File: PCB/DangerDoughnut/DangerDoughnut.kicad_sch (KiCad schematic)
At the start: 93 parts, among them J1 Conn_01x02_Pin, J2 Conn_01x02_Pin, J3 Conn_01x02_Pin, J4 Conn_01x04_Pin, J6 USB_C_Receptacle_USB2.0_16P, SW1 SW_Push, SW2 SW_Push, U1 MMC5983MA, U10 ESP32-S3, U2 H3LIS331DLTR, U3 H3LIS331DLTR, U4 W25X20CLZP, U6 L5973D, U7 MIC5219-3.3YM5, U8 ESP8285H16, U9 SX1280IMLTRT, Y1 40MHz, Y2 52MHz, Y3 26MHz

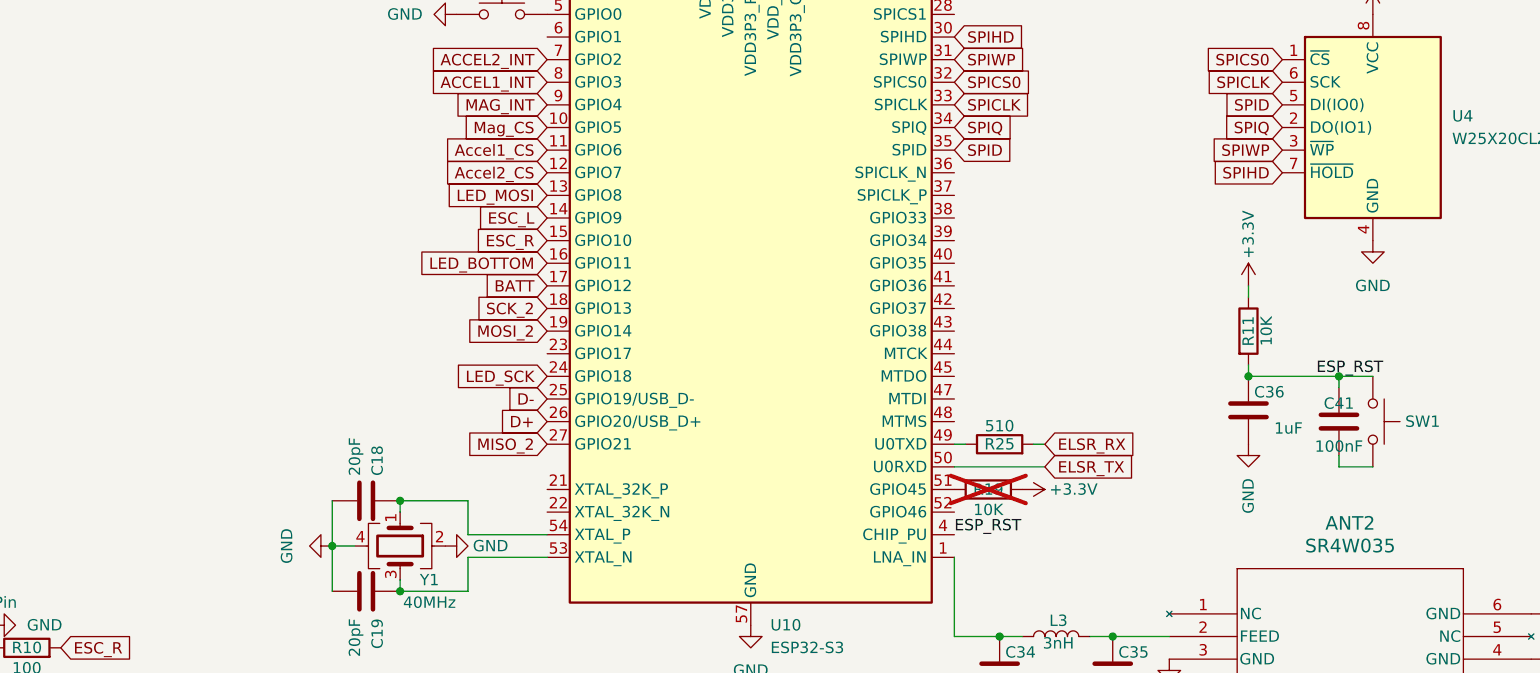
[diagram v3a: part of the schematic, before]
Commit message: updated layout
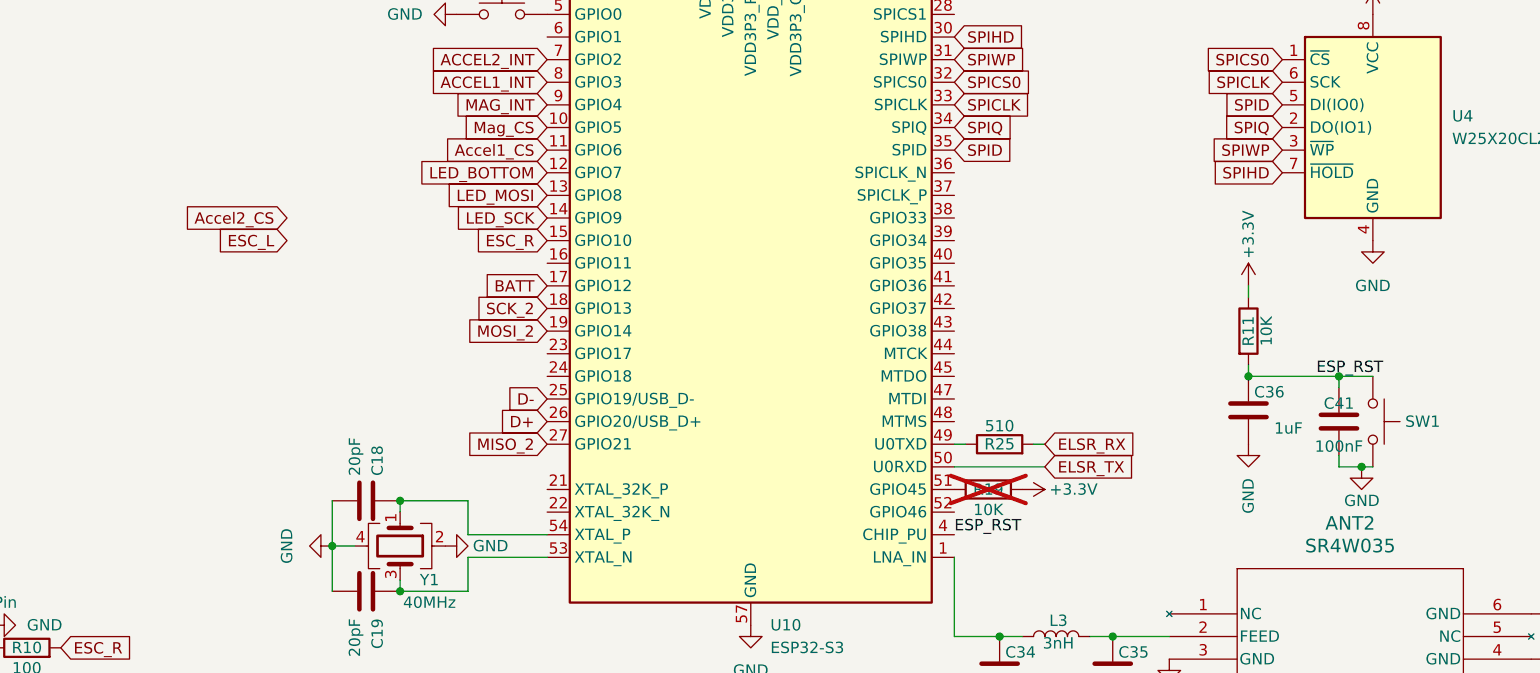
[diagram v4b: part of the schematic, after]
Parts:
- C29: footprint Capacitor_THT:CP_Radial_D6.3mm_P2.50mm -> Danger_Doughnut_Lib:CP_Right_Angle_D6.3_P2.50_H16.5
- SW1, SW2: footprint Button_Switch_SMD:SW_Push_1P1T_XKB_TS-1187A -> Danger_Doughnut_Lib:Pad_Button
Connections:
- net Accel2_CS: no longer U10.12 (GPIO7)
- net ESC_L: no longer U10.14 (GPIO9)
- net GND: now also C41.2, SW1.2
- net LED_BOTTOM: now also U10.12 (GPIO7); no longer U10.16 (GPIO11)
- net LED_SCK: now also U10.14 (GPIO9); no longer U10.24 (GPIO18)
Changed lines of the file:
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@@
 	)
 	(junction
+		(at 383.54 87.63)
+		(diameter 0)
+		(color 0 0 0 0)
+	)
+	(junction
 		(at 121.92 110.49)
 		(diameter 0)
@@
 	(wire
 		(pts
-			(xy 381 87.63) (xy 384.81 87.63)
+			(xy 381 87.63) (xy 383.54 87.63)
 		)
 		(stroke
@@
 	(wire
 		(pts
+			(xy 383.54 87.63) (xy 384.81 87.63)
+		)
+		(stroke
+			(width 0)
+			(type default)
+		)
+	)
+	(wire
+		(pts
 			(xy 318.77 222.25) (xy 317.5 222.25)
 		)
@@
 	(global_label "LED_BOTTOM"
 		(shape input)
-		(at 292.1 64.77 180)
+		(at 292.1 54.61 180)
 		(fields_autoplaced yes)
 		(effects
@@
 		)
 		(property "Intersheetrefs" "${INTERSHEET_REFS}"
-			(at 277.3825 64.77 0)
+			(at 277.3825 54.61 0)
 			(effects
 				(font
@@
 	(global_label "ESC_L"
 		(shape input)
-		(at 292.1 59.69 180)
+		(at 262.89 62.23 180)
 		(fields_autoplaced yes)
 		(effects
@@
 		)
 		(property "Intersheetrefs" "${INTERSHEET_REFS}"
-			(at 283.4906 59.69 0)
+			(at 254.2806 62.23 0)
 			(effects
 				(font
@@
 	(global_label "Accel2_CS"
 		(shape input)
-		(at 292.1 54.61 180)
+		(at 262.89 59.69 180)
 		(fields_autoplaced yes)
 		(effects
@@
 		)
 		(property "Intersheetrefs" "${INTERSHEET_REFS}"
-			(at 279.4386 54.61 0)
+			(at 250.2286 59.69 0)
 			(effects
 				(font
@@
 	(global_label "LED_SCK"
 		(shape input)
-		(at 292.1 77.47 180)
+		(at 292.1 59.69 180)
 		(fields_autoplaced yes)
 		(effects
@@
 		)
 		(property "Intersheetrefs" "${INTERSHEET_REFS}"
-			(at 280.9506 77.47 0)
+			(at 280.9506 59.69 0)
 			(effects
 				(font
@@
 			)
 		)
-		(property "Footprint" "Capacitor_THT:CP_Radial_D6.3mm_P2.50mm"
+		(property "Footprint" "Danger_Doughnut_Lib:CP_Right_Angle_D6.3_P2.50_H16.5"
 			(at 58.1152 224.79 0)
 			(effects
@@
 	)
 	(symbol
+		(lib_id "power:GND")
+		(at 383.54 87.63 0)
+		(unit 1)
+		(exclude_from_sim no)
+		(in_bom yes)
+		(on_board yes)
+		(dnp no)
+		(property "Reference" "#PWR0105"
+			(at 383.54 93.98 0)
+			(effects
+				(font
+					(size 1.27 1.27)
+				)
+				(hide yes)
+			)
+		)
+		(property "Value" "GND"
+			(at 385.572 91.44 0)
+			(effects
+				(font
+					(size 1.27 1.27)
+				)
+				(justify right)
+			)
+		)
+		(property "Footprint" ""
+			(at 383.54 87.63 0)
+			(effects
+				(font
+					(size 1.27 1.27)
+				)
+				(hide yes)
+			)
+		)
+		(property "Datasheet" ""
+			(at 383.54 87.63 0)
+			(effects
+				(font
+					(size 1.27 1.27)
+				)
+				(hide yes)
+			)
+		)
+		(property "Description" "Power symbol creates a global label with name \"GND\" , ground"
+			(at 383.54 87.63 0)
+			(effects
+				(font
+					(size 1.27 1.27)
+				)
+				(hide yes)
+			)
+		)
+		(pin "1"
+		)
+		(instances
+			(project "DangerDoughnut"
+				(path "/4036fe7f-48e1-40e6-b3b7-d8935a605c7b"
+					(reference "#PWR0105")
+					(unit 1)
+				)
+			)
+		)
+	)
+	(symbol
 		(lib_id "Device:C")
 		(at 353.06 22.86 0)
@@
 			)
 		)
-		(property "Footprint" "Button_Switch_SMD:SW_Push_1P1T_XKB_TS-1187A"
+		(property "Footprint" "Danger_Doughnut_Lib:Pad_Button"
 			(at 287.02 31.75 0)
 			(effects
@@
 			)
 		)
-		(property "Footprint" "Button_Switch_SMD:SW_Push_1P1T_XKB_TS-1187A"
+		(property "Footprint" "Danger_Doughnut_Lib:Pad_Button"
 			(at 389.89 82.55 0)
 			(effects

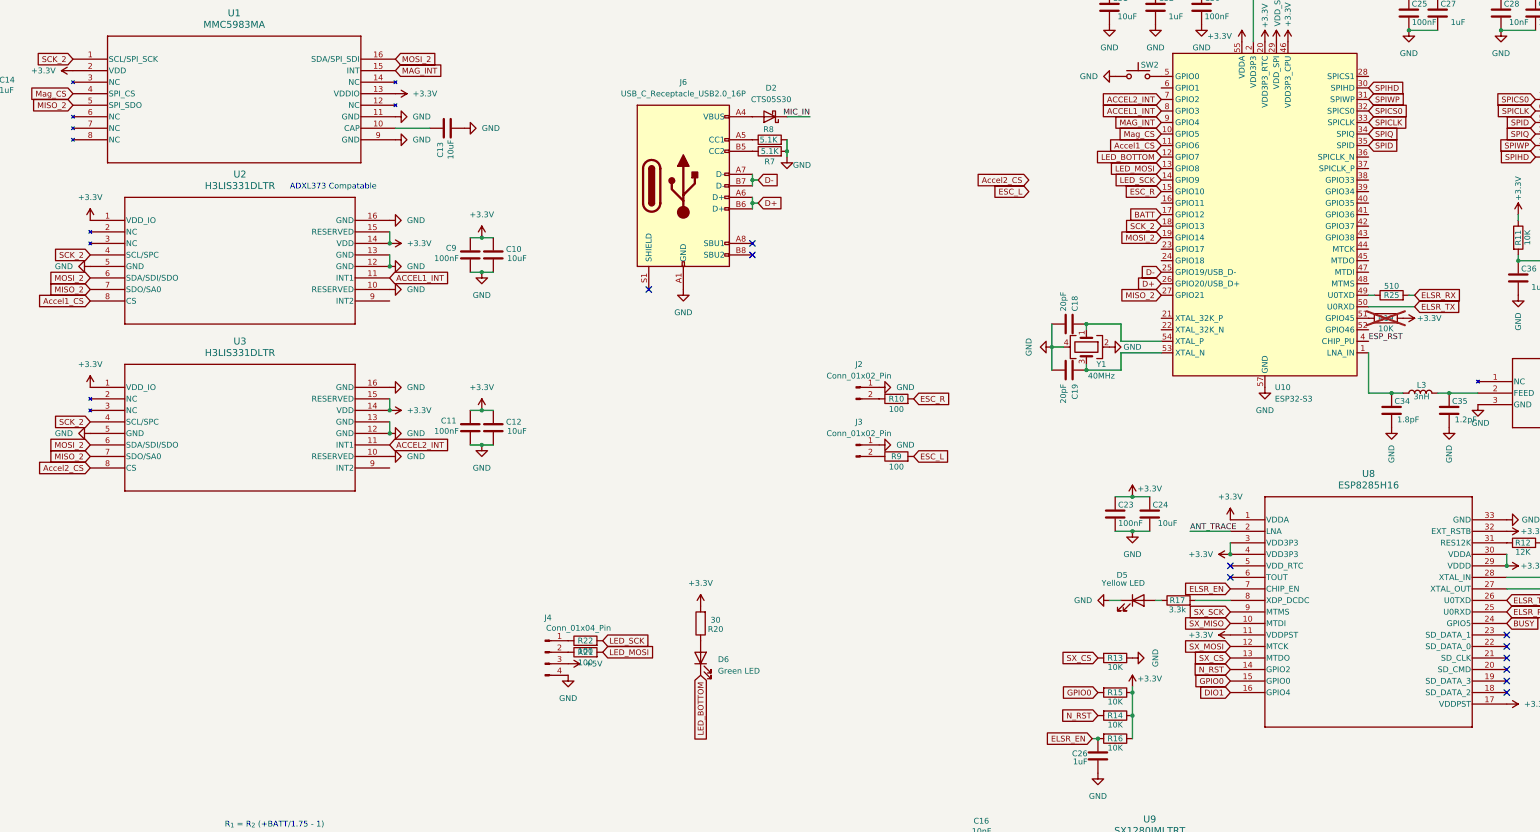
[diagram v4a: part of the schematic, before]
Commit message: updated layout needs 3v3 headers testpoints and verify
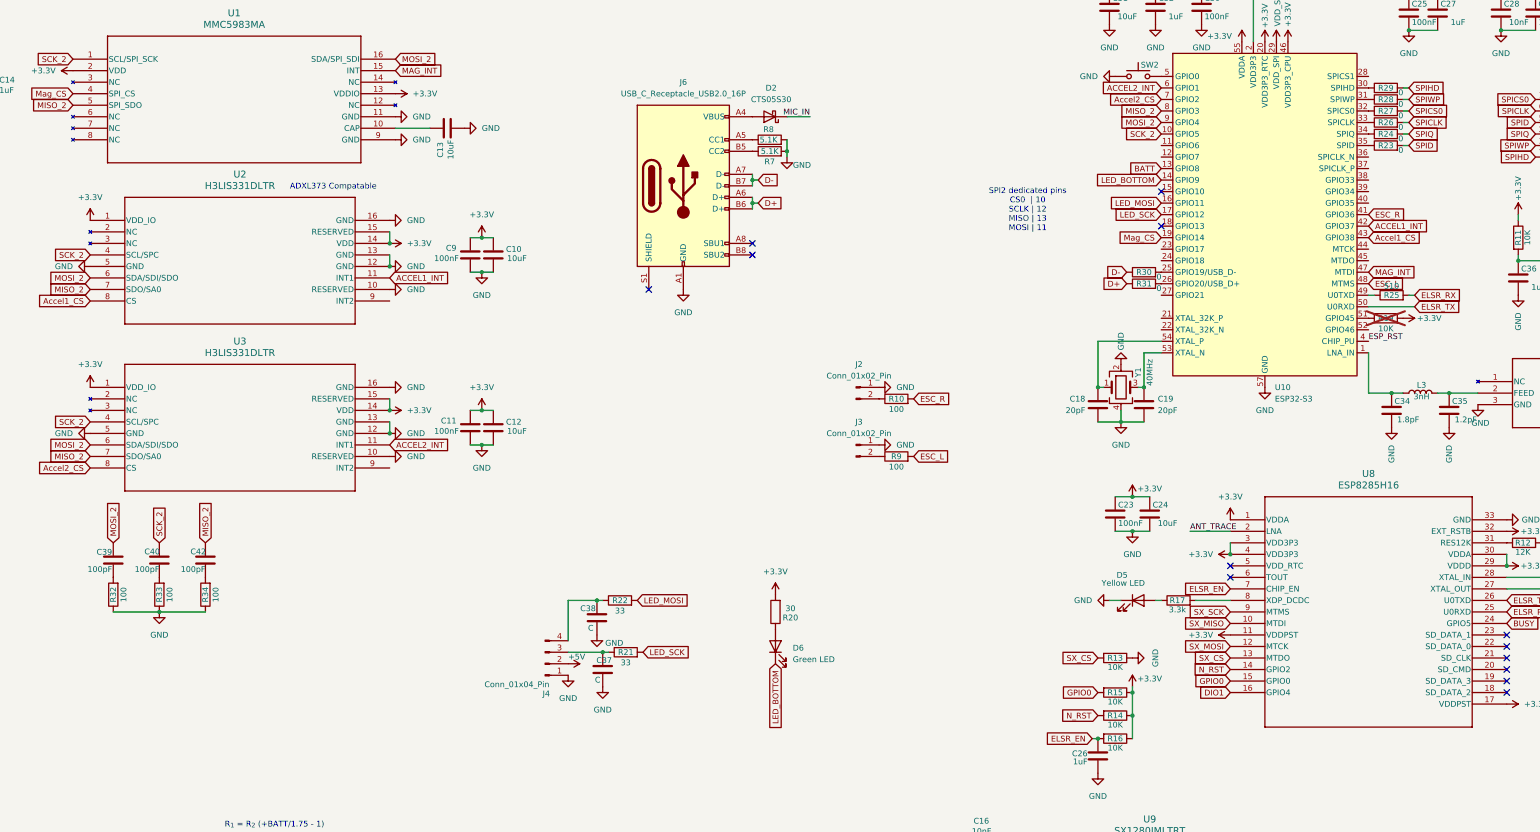
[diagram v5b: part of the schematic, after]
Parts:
- added C37, C38: C, Capacitor_SMD:C_0402_1005Metric, symbol Device:C
- added C39, C40, C42: 100pF, Capacitor_SMD:C_0402_1005Metric, symbol Device:C
- added R23, R24, R26, R27, R28, R29, R30, R31: 0, Resistor_SMD:R_0402_1005Metric, symbol Device:R
- added R32, R33, R34: 100, Resistor_SMD:R_0402_1005Metric, symbol Device:R
- R21, R22: value 100 -> 33
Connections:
- net +5V: now also J4.2 (Pin_2); no longer J4.3 (Pin_3)
- net ACCEL1_INT: now also U10.42 (GPIO37); no longer U10.8 (GPIO3)
- net ACCEL2_INT: now also U10.6 (GPIO1); no longer U10.7 (GPIO2)
- net Accel1_CS: now also U10.43 (GPIO38); no longer U10.11 (GPIO6)
- net Accel2_CS: now also U10.7 (GPIO2)
- net BATT: now also U10.13 (GPIO8); no longer U10.17 (GPIO12)
- net D+: now also R31.1; no longer U10.26 (GPIO20/USB_D+)
- net D-: now also R30.1; no longer U10.25 (GPIO19/USB_D-)
- net ESC_L: now also U10.48 (MTMS)
- net ESC_R: now also U10.41 (GPIO36); no longer U10.15 (GPIO10)
- net GND: now also J4.1 (Pin_1), C37.2, C38.2, R32.1, R33.1, R34.1; no longer J4.4 (Pin_4)
- net LED_BOTTOM: now also U10.14 (GPIO9); no longer U10.12 (GPIO7)
- net LED_MOSI: now also R22.2, U10.16 (GPIO11); no longer R21.2, U10.13 (GPIO8)
- net LED_SCK: now also R21.2, U10.17 (GPIO12); no longer R22.2, U10.14 (GPIO9)
- net MAG_INT: now also U10.47 (MTDI); no longer U10.9 (GPIO4)
- net MISO_2: now also U10.8 (GPIO3), C42.1; no longer U10.27 (GPIO21)
- net MOSI_2: now also U10.9 (GPIO4), C39.1; no longer U10.19 (GPIO14)
- net Mag_CS: now also U10.19 (GPIO14); no longer U10.10 (GPIO5)
- net SCK_2: now also U10.10 (GPIO5), C40.1; no longer U10.18 (GPIO13)
- net SPICLK: now also R26.2; no longer U10.33 (SPICLK)
- net SPICS0: now also R27.2; no longer U10.32 (SPICS0)
- net SPID: now also R23.2; no longer U10.35 (SPID)
- net SPIHD: now also R29.2; no longer U10.30 (SPIHD)
- net SPIQ: now also R24.2; no longer U10.34 (SPIQ)
- net SPIWP: now also R28.2; no longer U10.31 (SPIWP)
- net at R22.1: now also J4.4 (Pin_4), C38.1; no longer J4.1 (Pin_1)
- net at R21.1: now also J4.3 (Pin_3), C37.1; no longer J4.2 (Pin_2)
- new net: C39.2, R32.2
- new net: R30.2, U10.25 (GPIO19/USB_D-)
- new net: R31.2, U10.26 (GPIO20/USB_D+)
- new net: R29.1, U10.30 (SPIHD)
- new net: R28.1, U10.31 (SPIWP)
- new net: R27.1, U10.32 (SPICS0)
- new net: R26.1, U10.33 (SPICLK)
- new net: R24.1, U10.34 (SPIQ)
- new net: R23.1, U10.35 (SPID)
- new net: C42.2, R34.2
- new net: C40.2, R33.2
- no-connect marks 18 -> 20
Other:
- note added: "SPI2 dedicated pins CS0 | 10 SCLK | 12 MISO | 13 MOSI | 11"
- moved on the sheet: C18, C19, D6, R20, R21, R22, Y1

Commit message: esp32 pins checked
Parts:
- added J5: TC2030-NL, Connector:Tag-Connect_TC2030-IDC-NL_2x03_P1.27mm_Vertical, symbol Connector:Conn_ARM_SWD_TagConnect_TC2030-NL
- added R35: 510, Resistor_SMD:R_0402_1005Metric, symbol Device:R
- added R36: 10K, Resistor_SMD:R_0402_1005Metric, symbol Device:R
- added TP2: 5v, TestPoint:TestPoint_Pad_D1.0mm, symbol Connector:TestPoint
- added TP3: 3v3, TestPoint:TestPoint_Pad_D1.0mm, symbol Connector:TestPoint
- added TP4: Batt_sens, TestPoint:TestPoint_Pad_D1.0mm, symbol Connector:TestPoint
- R10, R9: value 100 -> 33
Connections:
- net +3.3V: now also J5.1 (VCC), TP3.1
- net +5V: now also TP2.1
- net ACCEL1_INT: now also U10.41 (GPIO36); no longer U10.42 (GPIO37)
- net Accel1_CS: now also U10.42 (GPIO37); no longer U10.43 (GPIO38)
- net BATT: now also U10.19 (GPIO14), TP4.1; no longer U10.13 (GPIO8)
- net ELSR_TX: now also R35.2; no longer U8.26 (U0TXD)
- net ESC_L: now also J3.2 (Pin_2); no longer U10.48 (MTMS)
- net ESC_R: now also J2.2 (Pin_2); no longer U10.41 (GPIO36)
- net ESP_RST: now also J5.3 (~{RESET})
- net GND: now also J5.5 (GND), R36.2
- net MAG_INT: now also U10.39 (GPIO34); no longer U10.47 (MTDI)
- net Mag_CS: now also U10.38 (GPIO33); no longer U10.19 (GPIO14)
- net at R9.1: now also U10.43 (GPIO38); no longer J3.2 (Pin_2)
- net at R10.1: now also U10.40 (GPIO35); no longer J2.2 (Pin_2)
- net at U10.52 (GPIO46): now also R36.1
- new net: R35.1, U8.26 (U0TXD)
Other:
- note added: "Header pins: extra esp pins ESP UART ELSR serial lines spi1 spi2 ESCs"
- moved on the sheet: C15, C5, R10, R9, Y3

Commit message: test points done
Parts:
- removed J5: TC2030-NL, Connector:Tag-Connect_TC2030-IDC-NL_2x03_P1.27mm_Vertical, symbol Connector:Conn_ARM_SWD_TagConnect_TC2030-NL
- added J10, J11, J12, J13, J14, J15, J16, J17, J19, J20, J7, J8, J9: Conn_01x01_Pin, Connector_Wire:SolderWirePad_1x01_SMD_1x2mm, symbol Connector:Conn_01x01_Pin
- added JP1: SolderJumper_2_Open, Jumper:SolderJumper-2_P1.3mm_Open_RoundedPad1.0x1.5mm, symbol Jumper:SolderJumper_2_Open
- added TP10: A1_CS, Danger_Doughnut_Lib:Test_Via, symbol Connector:TestPoint
- added TP11: A1_INT, Danger_Doughnut_Lib:Test_Via, symbol Connector:TestPoint
- added TP12: A2_CS, Danger_Doughnut_Lib:Test_Via, symbol Connector:TestPoint
- added TP13: A2_INT, Danger_Doughnut_Lib:Test_Via, symbol Connector:TestPoint
- added TP14: MAG_CS, Danger_Doughnut_Lib:Test_Via, symbol Connector:TestPoint
- added TP15: MAG_INT, Danger_Doughnut_Lib:Test_Via, symbol Connector:TestPoint
- added TP16: BATT, Danger_Doughnut_Lib:Test_Via, symbol Connector:TestPoint
- added TP17: SX_MOSI, Danger_Doughnut_Lib:Test_Via_small, symbol Connector:TestPoint
- added TP18: LED_MOSI, Danger_Doughnut_Lib:Test_Via, symbol Connector:TestPoint
- added TP19: LED_SCK, Danger_Doughnut_Lib:Test_Via, symbol Connector:TestPoint
- added TP20: ESC_L, Danger_Doughnut_Lib:Test_Via, symbol Connector:TestPoint
- added TP21: ESC_R, Danger_Doughnut_Lib:Test_Via, symbol Connector:TestPoint
- added TP22: SX_SCK, Danger_Doughnut_Lib:Test_Via_small, symbol Connector:TestPoint
- added TP23: SX_CS, Danger_Doughnut_Lib:Test_Via_small, symbol Connector:TestPoint
- added TP24: Busy, Danger_Doughnut_Lib:Test_Via_small, symbol Connector:TestPoint
- added TP25: RST, Danger_Doughnut_Lib:Test_Via_small, symbol Connector:TestPoint
- added TP26: 5v, Danger_Doughnut_Lib:Test_Via, symbol Connector:TestPoint
- added TP27: 3v3, Danger_Doughnut_Lib:Test_Via, symbol Connector:TestPoint
- added TP28: GND, Danger_Doughnut_Lib:Test_Via, symbol Connector:TestPoint
- added TP5: MISO, Danger_Doughnut_Lib:Test_Via, symbol Connector:TestPoint
- added TP6: MOSI, Danger_Doughnut_Lib:Test_Via, symbol Connector:TestPoint
- added TP7: SCK, Danger_Doughnut_Lib:Test_Via, symbol Connector:TestPoint
- added TP8: ELSR_TX, Danger_Doughnut_Lib:Test_Via, symbol Connector:TestPoint
- added TP9: ELSR_RX, Danger_Doughnut_Lib:Test_Via, symbol Connector:TestPoint
- TP4: value Batt_sens -> SX_MISO; footprint TestPoint:TestPoint_Pad_D1.0mm -> Danger_Doughnut_Lib:Test_Via_small
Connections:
- net +3.3V: now also J12.1 (Pin_1), J17.1 (Pin_1), TP27.1
- net +5V: now also J14.1 (Pin_1), TP26.1
- net ACCEL1_INT: now also TP11.1
- net ACCEL2_INT: now also TP13.1
- net Accel1_CS: now also TP10.1
- net Accel2_CS: now also TP12.1
- net BATT: now also TP16.1; no longer TP4.1
- net BUSY: now also TP24.1
- net ELSR_RX: now also TP9.1
- net ELSR_TX: now also TP8.1
- net ESC_L: now also TP20.1
- net ESC_R: now also TP21.1
- net GND: now also J15.1 (Pin_1), J19.1 (Pin_1), J20.1 (Pin_1), JP1.1 (A), TP28.1
- net GPIO0: now also JP1.2 (B)
- net MAG_INT: now also TP15.1
- net MISO_2: now also TP5.1
- net MOSI_2: now also TP6.1
- net Mag_CS: now also TP14.1
- net N_RST: now also TP25.1
- net SCK_2: now also TP7.1
- net SX_CS: now also TP23.1
- net SX_MISO: now also TP4.1
- net SX_MOSI: now also TP17.1
- net SX_SCK: now also TP22.1
- net at C38.1, J4.4 (Pin_4), R22.1: now also TP18.1
- net at U10.11 (GPIO6): now also J7.1 (Pin_1)
- net at U10.12 (GPIO7): now also J8.1 (Pin_1)
- net at U10.13 (GPIO8): now also J9.1 (Pin_1)
- net at U10.23 (GPIO17): now also J10.1 (Pin_1)
- net at U10.24 (GPIO18): now also J11.1 (Pin_1)
- net at U10.44 (MTCK): now also J13.1 (Pin_1)
- net at U10.48 (MTMS): now also J16.1 (Pin_1)
- net at C37.1, J4.3 (Pin_3), R21.1: now also TP19.1
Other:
- note added: "TODO: Organize"
- note removed: "Header pins: extra esp pins ESP UART ELSR serial lines spi1 spi2 ESCs"
- note removed: "TODO: add pin header add disconnects add test points add ground option elrs boot pin boot pins accessable Organize"

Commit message: Layout Done
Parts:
- added C43, C44: 20pF, Capacitor_SMD:C_0402_1005Metric_Pad0.74x0.62mm_HandSolder, symbol Device:C
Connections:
- net GND: now also J11.1 (Pin_1), C43.1, C44.1
- net at U10.24 (GPIO18): no longer J11.1 (Pin_1)
- net at U9.4 (XTA), Y2.1: now also C43.2
- net at U9.6 (XTB), Y2.3: now also C44.2
- no-connect marks 20 -> 22
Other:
- moved on the sheet: J11
